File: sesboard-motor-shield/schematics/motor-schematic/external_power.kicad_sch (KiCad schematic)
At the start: 14 parts, among them J1 Barrel_Jack, Q1 Q_NMOS_DGS, Q2 TIP3055, U1 LM317_SOT-223, U4 AMS1117-5.0

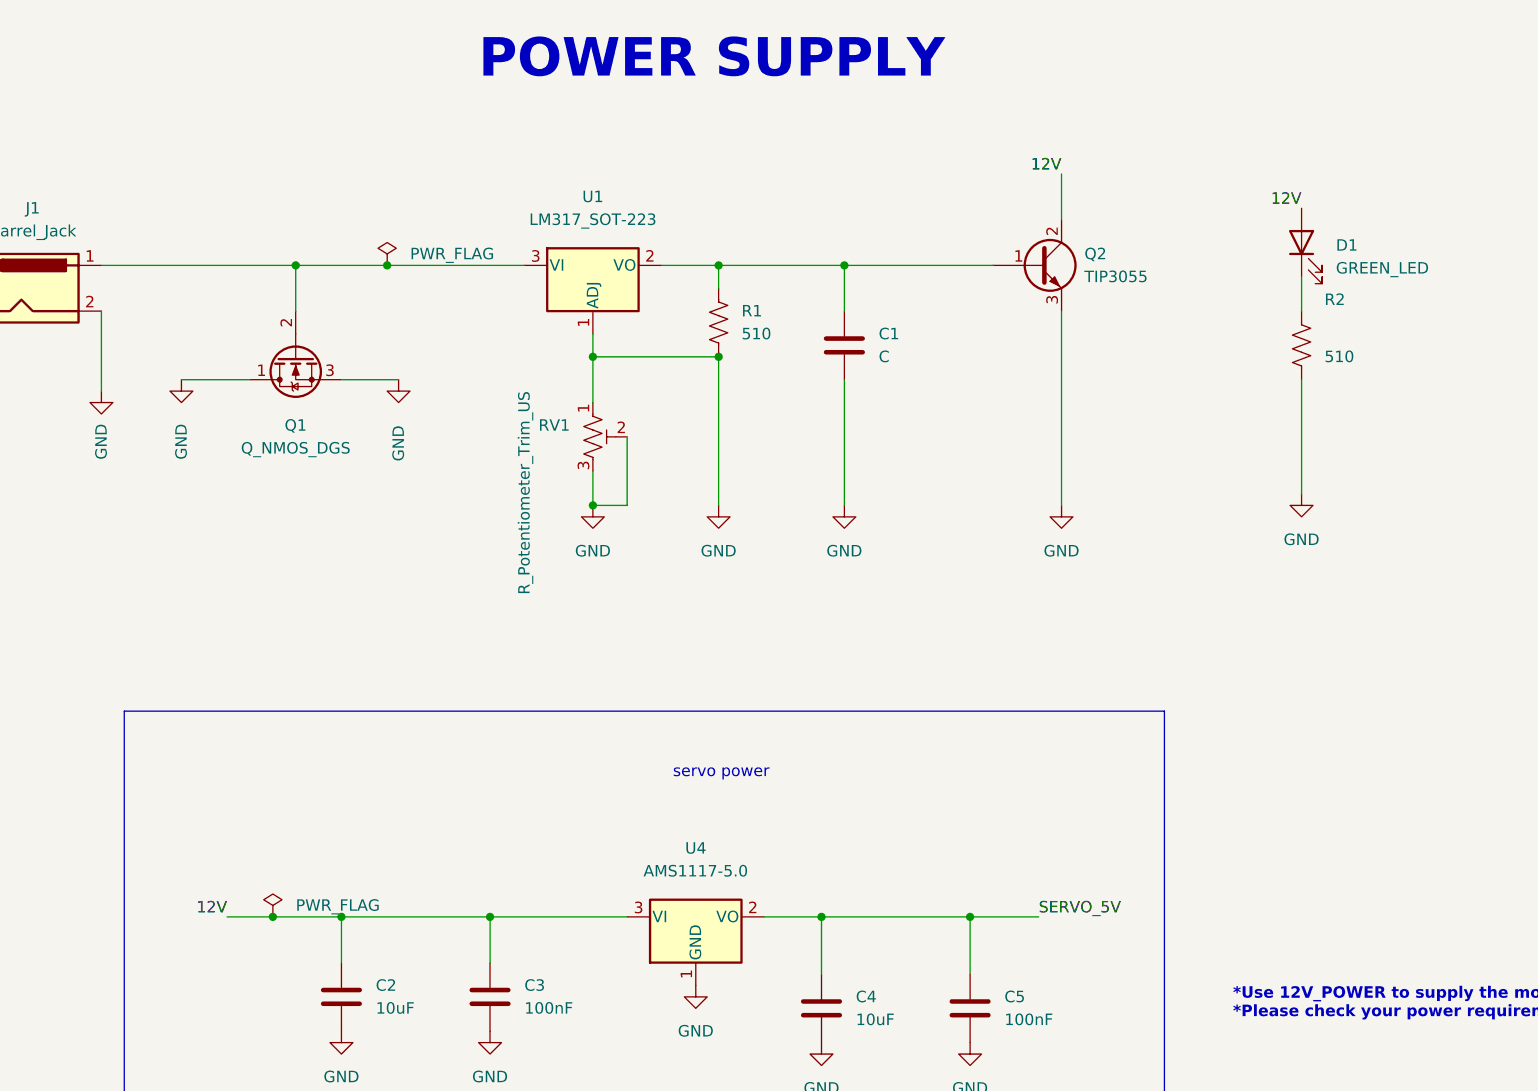
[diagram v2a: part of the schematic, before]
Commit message: added global labels for motor drivers
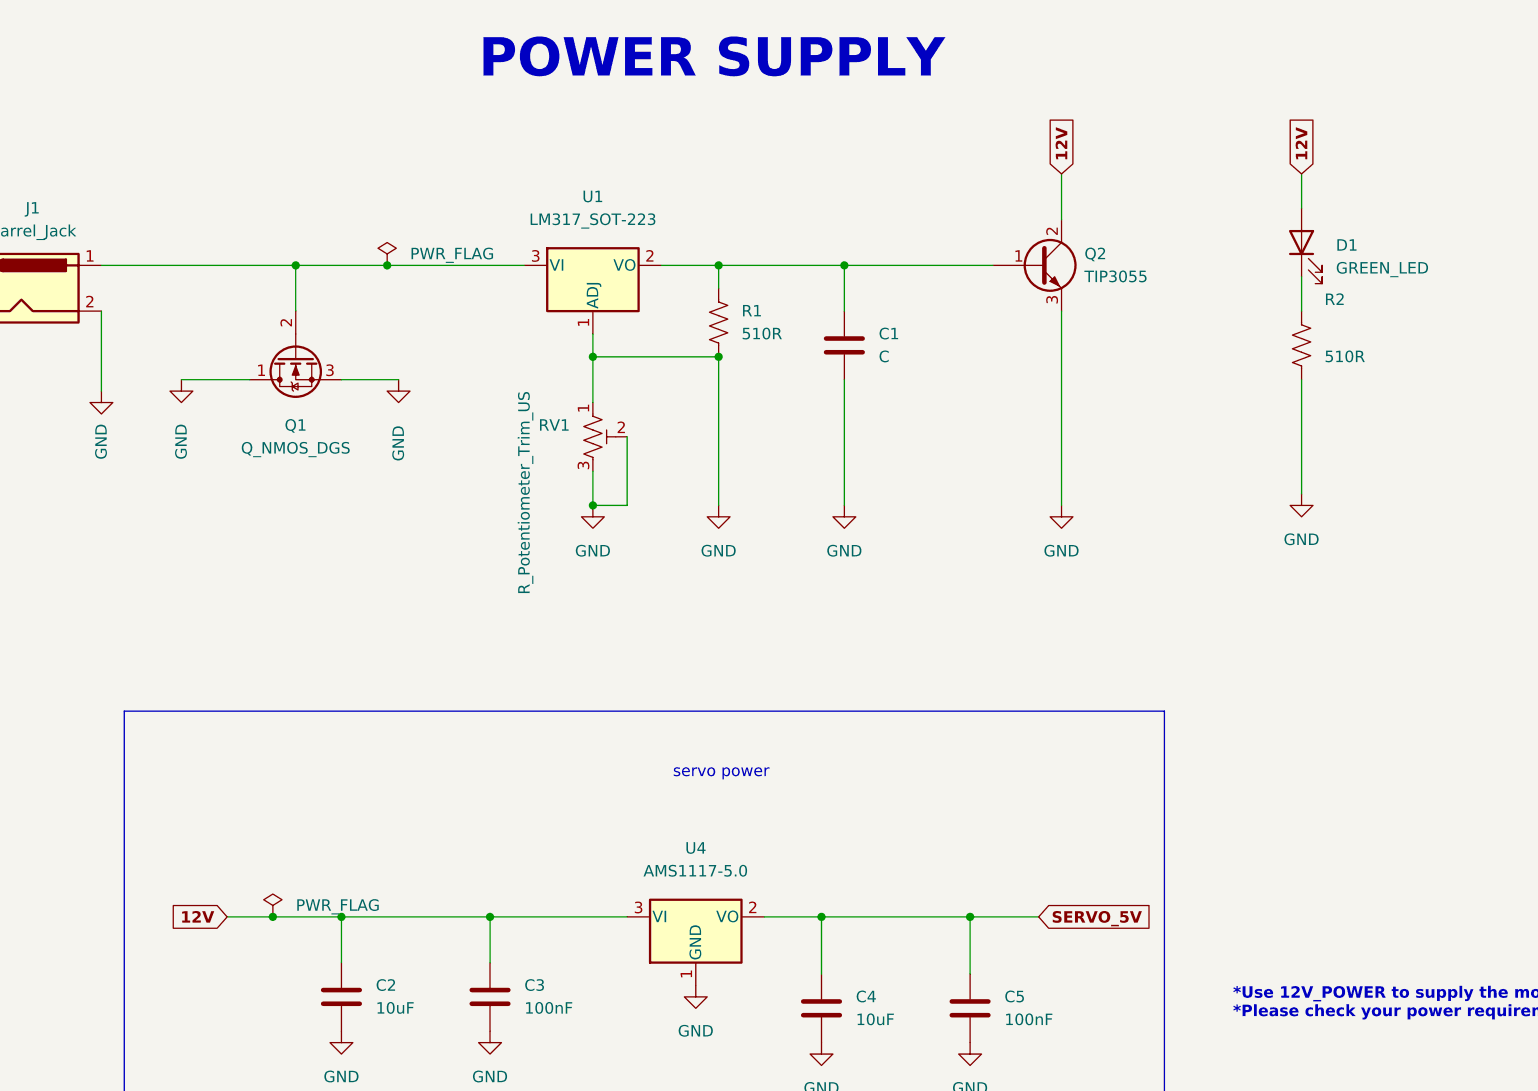
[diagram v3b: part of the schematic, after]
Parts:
- C1, C2, C3, C4: footprint (none) -> Capacitor_SMD:C_0603_1608Metric
- C5: footprint (none) -> Capacitor_SMD:C_0603_1608Metric_Pad1.08x0.95mm_HandSolder
- D1: footprint (none) -> LED_SMD:LED_0603_1608Metric
- J1: footprint (none) -> Connector_BarrelJack:BarrelJack_Horizontal
- Q1: footprint (none) -> Package_TO_SOT_THT:TO-220-3_Vertical
- R1, R2: value 510 -> 510R; footprint (none) -> Resistor_SMD:R_0603_1608Metric
- RV1: footprint (none) -> Potentiometer_SMD:Potentiometer_Vishay_TS53YL_Vertical
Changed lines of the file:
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@@
+    (stroke (width 0) (type default) (color 0 0 0 0))
+  )
+  (wire (pts (xy 210.82 31.75) (xy 210.82 35.56))
     (stroke (width 0) (type default) (color 0 0 0 0))
   )
@@
     (effects (font (size 1.27 1.27)) (justify left bottom))
   )
-  (label "12V" (at 210.82 35.56 180)
-    (effects (font (size 1.27 1.27)) (justify right bottom))
-  )
-  (label "SERVO_5V" (at 181.61 114.3 0)
-    (effects (font (size 1.27 1.27)) (justify left bottom))
-  )
-  (label "12V" (at 184.15 31.75 180)
-    (effects (font (size 1.27 1.27)) (justify right bottom))
-  )
-  (label "12V" (at 91.44 114.3 180)
-    (effects (font (size 1.27 1.27)) (justify right bottom))
+  (global_label "12V" (shape input) (at 210.82 31.75 90) (fields_autoplaced)
+    (effects (font (size 1.27 1.27) bold) (justify left))
+    (property "Intersheet References" "${INTERSHEET_REFS}" (id 0) (at 210.693 25.6389 90)
+      (effects (font (size 1.27 1.27) bold) (justify left) hide)
+    )
+  )
+  (global_label "SERVO_5V" (shape input) (at 181.61 114.3 0) (fields_autoplaced)
+    (effects (font (size 1.27 1.27) bold) (justify left))
+    (property "Intersheet References" "${INTERSHEET_REFS}" (id 0) (at 193.5268 114.173 0)
+      (effects (font (size 1.27 1.27) bold) (justify left) hide)
+    )
+  )
+  (global_label "12V" (shape input) (at 184.15 31.75 90) (fields_autoplaced)
+    (effects (font (size 1.27 1.27) bold) (justify left))
+    (property "Intersheet References" "${INTERSHEET_REFS}" (id 0) (at 184.023 25.6389 90)
+      (effects (font (size 1.27 1.27) bold) (justify left) hide)
+    )
+  )
+  (global_label "12V" (shape input) (at 91.44 114.3 180) (fields_autoplaced)
+    (effects (font (size 1.27 1.27) bold) (justify right))
+    (property "Intersheet References" "${INTERSHEET_REFS}" (id 0) (at 85.3289 114.427 0)
+      (effects (font (size 1.27 1.27) bold) (justify right) hide)
+    )
   )
   (symbol (lib_id "Device:LED") (at 210.82 39.37 90) (unit 1)
@@
       (effects (font (size 1.27 1.27)) (justify right))
     )
-    (property "Footprint" "" (id 2) (at 210.82 39.37 0)
+    (property "Footprint" "LED_SMD:LED_0603_1608Metric" (id 2) (at 210.82 39.37 0)
       (effects (font (size 1.27 1.27)) hide)
     )
@@
       (effects (font (size 1.27 1.27)) (justify left))
     )
-    (property "Value" "510" (id 1) (at 213.36 52.0699 0)
-      (effects (font (size 1.27 1.27)) (justify left))
-    )
-    (property "Footprint" "" (id 2) (at 211.836 51.054 90)
+    (property "Value" "510R" (id 1) (at 213.36 52.0699 0)
+      (effects (font (size 1.27 1.27)) (justify left))
+    )
+    (property "Footprint" "Resistor_SMD:R_0603_1608Metric" (id 2) (at 211.836 51.054 90)
       (effects (font (size 1.27 1.27)) hide)
     )
@@
       (effects (font (size 1.27 1.27)) (justify left))
     )
-    (property "Footprint" "" (id 2) (at 158.4452 128.27 0)
+    (property "Footprint" "Capacitor_SMD:C_0603_1608Metric" (id 2) (at 158.4452 128.27 0)
       (effects (font (size 1.27 1.27)) hide)
     )
@@
       (effects (font (size 1.27 1.27)) (justify left))
     )
-    (property "Footprint" "" (id 2) (at 174.9552 128.27 0)
+    (property "Footprint" "Capacitor_SMD:C_0603_1608Metric_Pad1.08x0.95mm_HandSolder" (id 2) (at 174.9552 128.27 0)
       (effects (font (size 1.27 1.27)) hide)
     )
@@
     (property "Reference" "J1" (id 0) (at 69.85 35.56 0))
     (property "Value" "Barrel_Jack" (id 1) (at 69.85 38.1 0))
-    (property "Footprint" "" (id 2) (at 71.12 45.466 0)
+    (property "Footprint" "Connector_BarrelJack:BarrelJack_Horizontal" (id 2) (at 71.12 45.466 0)
       (effects (font (size 1.27 1.27)) hide)
     )
@@
       (effects (font (size 1.27 1.27)) (justify left))
     )
-    (property "Footprint" "" (id 2) (at 105.1052 127 0)
+    (property "Footprint" "Capacitor_SMD:C_0603_1608Metric" (id 2) (at 105.1052 127 0)
       (effects (font (size 1.27 1.27)) hide)
     )
@@
       (effects (font (size 1.27 1.27)) (justify left))
     )
-    (property "Footprint" "" (id 2) (at 121.6152 127 0)
+    (property "Footprint" "Capacitor_SMD:C_0603_1608Metric" (id 2) (at 121.6152 127 0)
       (effects (font (size 1.27 1.27)) hide)
     )
@@
     (property "Reference" "Q1" (id 0) (at 99.06 59.69 90))
     (property "Value" "Q_NMOS_DGS" (id 1) (at 99.06 62.23 90))
-    (property "Footprint" "" (id 2) (at 96.52 57.15 0)
+    (property "Footprint" "Package_TO_SOT_THT:TO-220-3_Vertical" (id 2) (at 96.52 57.15 0)
       (effects (font (size 1.27 1.27)) hide)
     )
@@
       (effects (font (size 1.27 1.27)) (justify left))
     )
-    (property "Footprint" "" (id 2) (at 160.9852 54.61 0)
+    (property "Footprint" "Capacitor_SMD:C_0603_1608Metric" (id 2) (at 160.9852 54.61 0)
       (effects (font (size 1.27 1.27)) hide)
     )
@@
       (effects (font (size 1.27 1.27)) (justify right))
     )
-    (property "Footprint" "" (id 2) (at 132.08 60.96 0)
+    (property "Footprint" "Potentiometer_SMD:Potentiometer_Vishay_TS53YL_Vertical" (id 2) (at 132.08 60.96 0)
       (effects (font (size 1.27 1.27)) hide)
     )
@@
       (effects (font (size 1.27 1.27)) (justify left))
     )
-    (property "Value" "510" (id 1) (at 148.59 49.5299 0)
-      (effects (font (size 1.27 1.27)) (justify left))
-    )
-    (property "Footprint" "" (id 2) (at 147.066 48.514 90)
-      (effects (font (size 1.27 1.27)) hide)
-    )
+    (property "Value" "510R" (id 1) (at 148.59 49.5299 0)
+      (effects (font (size 1.27 1.27)) (justify left))
+    )
+    (property "Footprint" "Resistor_SMD:R_0603_1608Metric" (id 2) (at 147.066 48.514 90)
+      (effects (font (size 1.27 1.27)) hide)
+    )

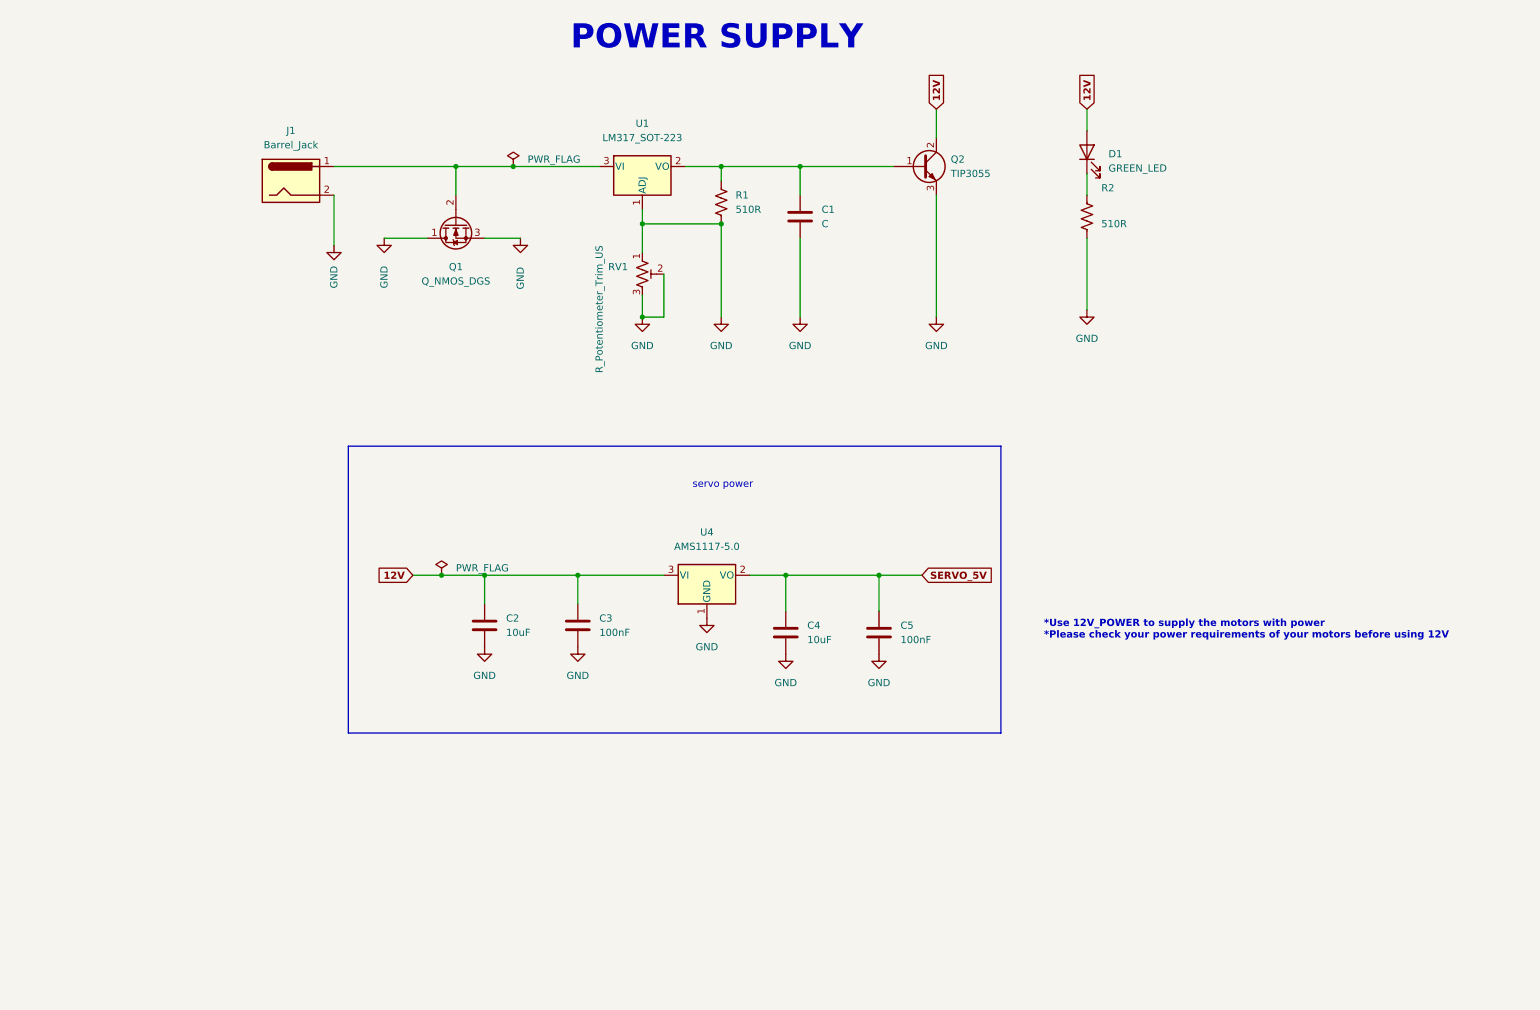
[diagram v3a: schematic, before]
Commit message: added power toggle
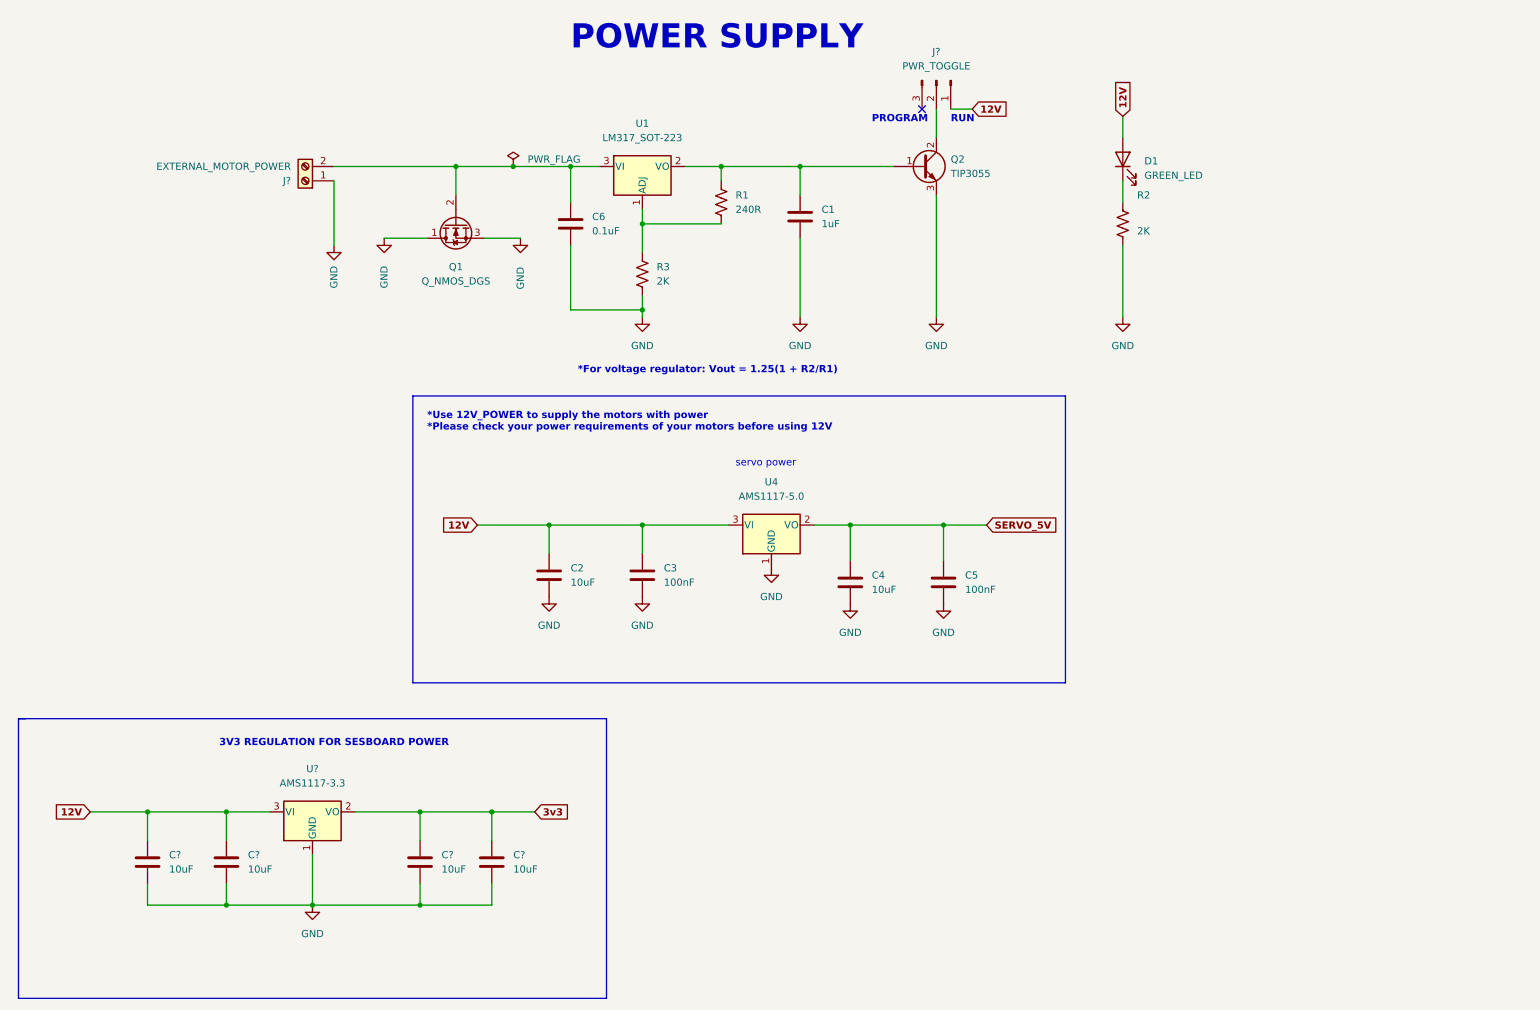
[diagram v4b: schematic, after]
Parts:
- removed J1: Barrel_Jack, Connector_BarrelJack:BarrelJack_Horizontal, symbol Connector:Barrel_Jack
- removed RV1: R_Potentiometer_Trim_US, Potentiometer_SMD:Potentiometer_Vishay_TS53YL_Vertical, symbol Device:R_Potentiometer_Trim_US
- added C6: 0.1uF, Capacitor_SMD:C_0603_1608Metric, symbol Device:C
- added C? (x4): 10uF, Capacitor_SMD:C_0603_1608Metric, symbol Device:C
- added J?: PWR_TOGGLE, symbol Connector:Conn_01x03_Male
- added J?: EXTERNAL_MOTOR_POWER, TerminalBlock_Phoenix:TerminalBlock_Phoenix_MKDS-1,5-2_1x02_P5.00mm_Horizontal, symbol Connector:Screw_Terminal_01x02
- added R3: 2K, Resistor_SMD:R_0603_1608Metric, symbol Device:R_US
- added U?: AMS1117-3.3, Package_TO_SOT_SMD:SOT-223-3_TabPin2, symbol Regulator_Linear:AMS1117-3.3
- C1: value C -> 1uF
- Q2: footprint Package_TO_SOT_THT:TO-218-3_Vertical -> Package_TO_SOT_THT:TO-220-3_Vertical
- R1: value 510R -> 240R
- R2: value 510R -> 2K
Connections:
- net 12V: now also C?.1, C?.1, J?.1 (Pin_1), U?.3 (VI); no longer Q2.2 (C)
- net GND: now also C6.2, C?.2, C?.2, C?.2, C?.2, J?.1 (Pin_1), R3.2, U?.1 (GND); no longer R1.2, U1.1 (ADJ)
- net at Q1.2 (G), U1.3 (VI): now also C6.1, J?.2 (Pin_2)
- new net: R1.2, R3.1, U1.1 (ADJ)
- new net: J?.2 (Pin_2), Q2.2 (C)
- new net 3v3: C?.1, C?.1, U?.2 (VO)
- no-connect marks 0 -> 1
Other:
- note added: "*For voltage regulator: Vout = 1.25(1 + R2/R1)"
- note added: "3V3 REGULATION FOR SESBOARD POWER"
- note added: "PROGRAM"
- note added: "RUN"
- moved on the sheet: C2, C3, C4, C5, D1, R2, U4
